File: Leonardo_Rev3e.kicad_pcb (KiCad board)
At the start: 2 copper layers, 68.6 x 53.3 mm, 61 parts, among them IC1 REG1117-5, IC2 LMV358IDGKR, J1 USBMICRO, J2 8x1F-H8.5, J3 8x1F-H8.5, J4 6x1F-H8.5, T1 FDN340P, U1 ATMEGA32U4-XUMU, U2 ATMEGA32U4-XUAU, U3 LP2985-33DBVR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

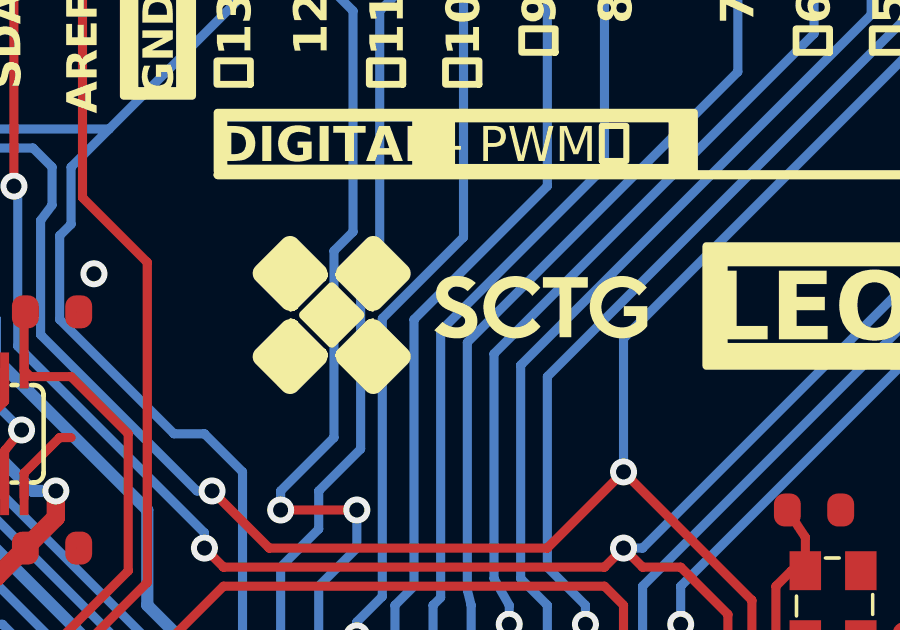
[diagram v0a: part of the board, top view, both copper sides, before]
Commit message: chore: adapt for forked repo
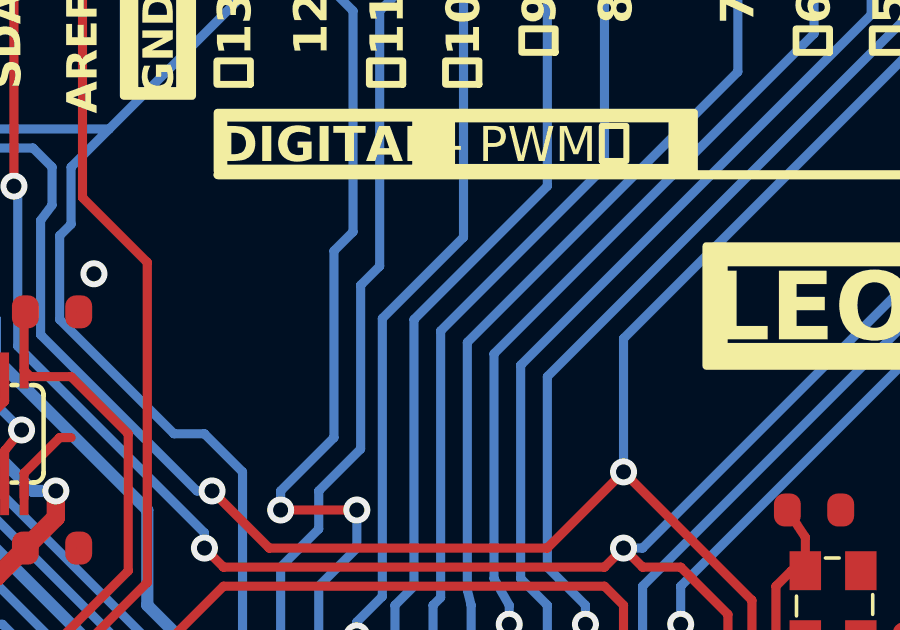
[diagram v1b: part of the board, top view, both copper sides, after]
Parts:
- removed REF**: Logo, Leonardo_Rev3e:Logo

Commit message: chore: clean up footprints
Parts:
- C1, C11, C13, C14, C2, C22, C3, C4, C5, C6, C7, C9: footprint Leonardo_Rev3e:C0603-ROUND -> Capacitor_SMD:C_0603_1608Metric_Pad1.08x0.95mm_HandSolder
- D1: footprint Leonardo_Rev3e:SMB -> Diode_SMD:D_SMB
- D2: footprint Leonardo_Rev3e:MINIMELF -> Diode_SMD:D_SOD-123
- IC1: footprint Leonardo_Rev3e:SOT223 -> Package_TO_SOT_SMD:SOT-223
- IC2: footprint Leonardo_Rev3e:MSOP08 -> Package_SO:MSOP-8_3x3mm_P0.65mm
- L1, L2: footprint Leonardo_Rev3e:0805 -> Resistor_SMD:R_0805_2012Metric_Pad1.20x1.40mm_HandSolder
- R1, R4: footprint Leonardo_Rev3e:R0603-ROUND -> Resistor_SMD:R_0603_1608Metric_Pad0.98x0.95mm_HandSolder
- R2, R3: footprint Leonardo_Rev3e:R0402 -> Resistor_SMD:R_0402_1005Metric_Pad0.72x0.64mm_HandSolder
- T1: footprint Leonardo_Rev3e:SOT-23 -> Package_TO_SOT_SMD:SOT-23
- U3: footprint Leonardo_Rev3e:SOT23-DBV -> Package_TO_SOT_SMD:SOT-23-5
- Z1, Z2: footprint Leonardo_Rev3e:CT_CN0603 -> Resistor_SMD:R_0603_1608Metric_Pad0.98x0.95mm_HandSolder
- moved D2 0.36 mm to (173.5, 105.0)
- moved C13 0.31 mm to (137.1, 101.5)
- turned IC1 to 180 degrees
- turned IC2 to 90 degrees
- turned T1 to 180 degrees
- turned U3 to 0 degrees
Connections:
- T1 pad 1: VUSB -> /GATE_CMD
- T1 pad 3: /GATE_CMD -> VUSB

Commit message: feat: use def. sym/foot and customised BOM and silkscreen
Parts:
- added G***: LOGO, Leonardo_Rev3e:Nexperia_X_Stamp_Logo_2x2mm, F.Cu at (133.8, 127.2)
- added G***: LOGO, Leonardo_Rev3e:Nexperia_X_Stamp_Logo_2x2mm, F.Cu at (132.2, 106.2)
- added G***: LOGO, Leonardo_Rev3e:Nexperia_X_Stamp_Logo_2x2mm, F.Cu at (173.5, 108.5)
- added REF**: OSHW-Logo2_14.6x12mm_SilkScreen, Symbol:OSHW-Logo2_14.6x12mm_SilkScreen, F.Cu at (149.8, 96.0)
- added REF**: WEEE-Logo_4.2x6mm_SilkScreen, Symbol:WEEE-Logo_4.2x6mm_SilkScreen, B.Cu at (134.8, 126.5)
- added REF**: OSHW-Logo2_14.6x12mm_SilkScreen, Symbol:OSHW-Logo2_14.6x12mm_SilkScreen, B.Cu at (164.2, 99.2)
- C1, C13, C2, C22, C6, C9: value 100n -> 100n-16V
- C10, C12, C8: value 10u -> 10u-16V; footprint Leonardo_Rev3e:SMC_B -> Capacitor_SMD:C_1206_3216Metric_Pad1.33x1.80mm_HandSolder
- C11, C14, C5, C7: value 1uF -> 1uF-16V
- C3, C4: value 22p -> 22p-10V
- D1: value M7 -> PMEG6020AELR; footprint Diode_SMD:D_SMB -> Diode_SMD:Nexperia_CFP3_SOD-123W
- D2: value 1N4148W-TP -> PMEG4005EH; footprint Diode_SMD:D_SOD-123 -> Diode_SMD:D_SOD-123F
- EXTPOWER0: footprint Leonardo_Rev3e:POWERSUPPLY_DC-21MM -> Leonardo_Rev3e:BarrelJack_Horizontal_Wurth_694108301002
- F1: value MF-MSMF050-2 500mA -> 500mA; footprint Leonardo_Rev3e:L1812 -> Fuse:Fuse_1812_4532Metric_Pad1.30x3.40mm_HandSolder
- IC1: value REG1117-5 -> LDI1117-05H
- IC2: value LMV358IDGKR -> LM358LVIDGKR
- J1: footprint Leonardo_Rev3e:10118194-0001LF -> Leonardo_Rev3e:Micro_USB_2.0_SMT_Type_B_Wurth_629105150521
- JP2: moved to B.Cu
- R2, R3: value NM -> 0
- RESET0: value TS07-667-30-BK-160-SMT-TR -> 431181015816; footprint Leonardo_Rev3e:TS07 -> Leonardo_Rev3e:PushButton_Wurth_431181015816
- RN1: value 10K -> 10k; footprint Leonardo_Rev3e:CAY16 -> Resistor_SMD:R_Cat16-4
- RN2: value 1K -> 1k; footprint Leonardo_Rev3e:CAY16 -> Resistor_SMD:R_Cat16-4
- RN3: footprint Leonardo_Rev3e:CAY16 -> Resistor_SMD:R_Cat16-4
- T1: value FDN340P -> NXV65UP
- U1: value ATMEGA32U4-XUMU -> ATMEGA32U4-MU
- U2: value ATMEGA32U4-XUAU -> ATMEGA32U4-AU
- U3: value LP2985-33DBVR -> LDI559-3.3EN
- Y1: value 16MHz KX-7 -> 16MHz
- moved EXTPOWER0 5.81 mm to (125.3, 123.8), turned to 0 degrees
- moved C10 5.01 mm to (137.0, 124.1)
- moved D1 2.06 mm to (133.8, 123.9)
- moved GND0 1.34 mm to (122.0, 96.5)
- moved JP2 1.29 mm to (119.8, 87.0)
- moved J1 1.12 mm to (117.2, 93.6)
- turned RESET0 to 0 degrees
- turned RN1 to 0 degrees
- turned RN2 to 180 degrees
- turned RN3 to 180 degrees
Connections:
- D1 pad 2: 3x2M_NM -> Net-(D1-A)
- EXTPOWER0 pad 1: 3x2M_NM -> Net-(D1-A)
- EXTPOWER0 pad 2: /VIN -> 3x2M_NM
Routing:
- net /RESET: track 189.6 -> 177.2 mm, vias 5 -> 3
- net /VIN: track 71.0 -> 59.4 mm, vias 2 -> 3
- net Net-(D1-A): track 0.00 -> 9.13 mm
- net /XUSB: track 15.1 -> 13.2 mm
- net 3x2M_NM: track 99.9 -> 101.8 mm, vias 21 -> 20
- net /D-: track 11.5 -> 9.91 mm
- net /D+: track 12.4 -> 10.8 mm
- net UGND: track 77.9 -> 76.4 mm
- net /USBID: track 13.0 -> 12.0 mm
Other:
- board text added: "OTG"
- board text removed: "-"
- board text removed: "2017-REV3e"
- board text removed: "original design: Leonardo board rev3d © Arduino s.r.l."
